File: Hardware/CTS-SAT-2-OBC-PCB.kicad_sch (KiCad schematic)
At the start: 0 parts

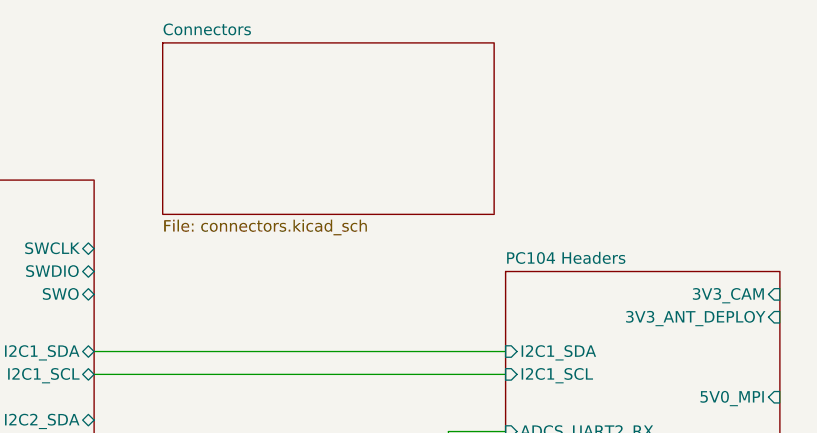
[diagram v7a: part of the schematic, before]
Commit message: Import CTS-SAT-1 PCB
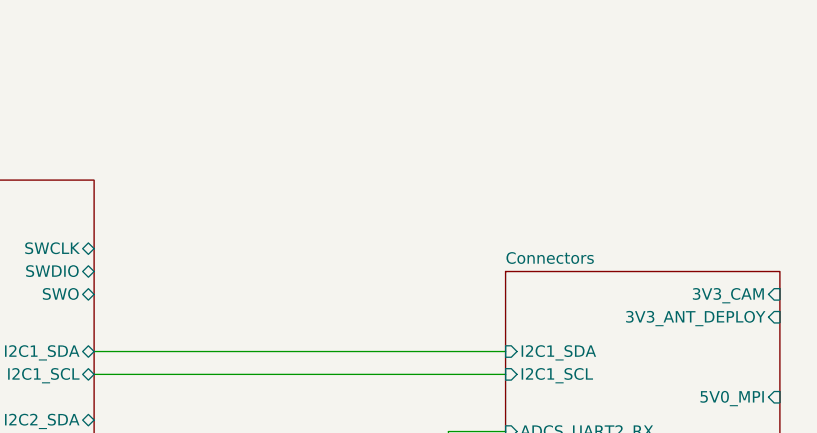
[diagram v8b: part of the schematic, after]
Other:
- removed sheet PC104 Headers
- sheet Connectors: file connectors.kicad_sch -> PC104.kicad_sch
- sheet Connectors ports: added 3V3_ANT_DEPLOY, 3V3_CAM, 5V0_MPI, ADCS_UART2_RX, ADCS_UART2_TX, I2C1_SCL, I2C1_SDA, VBAT_MONITOR; removed none
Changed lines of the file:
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@@
 			(color 0 0 0 0.0000)
 		)
-		(property "Sheetname" "PC104 Headers"
+		(property "Sheetname" "Connectors"
 			(at 248.92 66.5984 0)
 			(effects
@@
 				)
 			)
-		)
-	)
-	(sheet
-		(at 210.82 41.91)
-		(size 36.83 19.05)
-		(exclude_from_sim no)
-		(in_bom yes)
-		(on_board yes)
-		(dnp no)
-		(fields_autoplaced yes)
-		(stroke
-			(width 0.1524)
-			(type solid)
-		)
-		(fill
-			(color 0 0 0 0.0000)
-		)
-		(property "Sheetname" "Connectors"
-			(at 210.82 41.1984 0)
-			(effects
-				(font
-					(size 1.27 1.27)
-				)
-				(justify left bottom)
-			)
-		)
-		(property "Sheetfile" "connectors.kicad_sch"
-			(at 210.82 61.5446 0)
-			(effects
-				(font
-					(size 1.27 1.27)
-				)
-				(justify left top)
-			)
-		)
-		(instances
-			(project "CTS-SAT-2-OBC-PCB"
-				(path "/58243925-df8d-4fc1-899e-fce866d1d25a"
-					(page "6")
-				)
-			)
